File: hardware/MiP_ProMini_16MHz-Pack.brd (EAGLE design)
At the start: 41.4 x 63.8 mm, 52 parts, among them J2 AVR_ISP, Q1 16MHZ, U1 ATMEGA328, U2 MIC5205-5.0, U3 TS3USB221A, U4 MIC5205-3.3

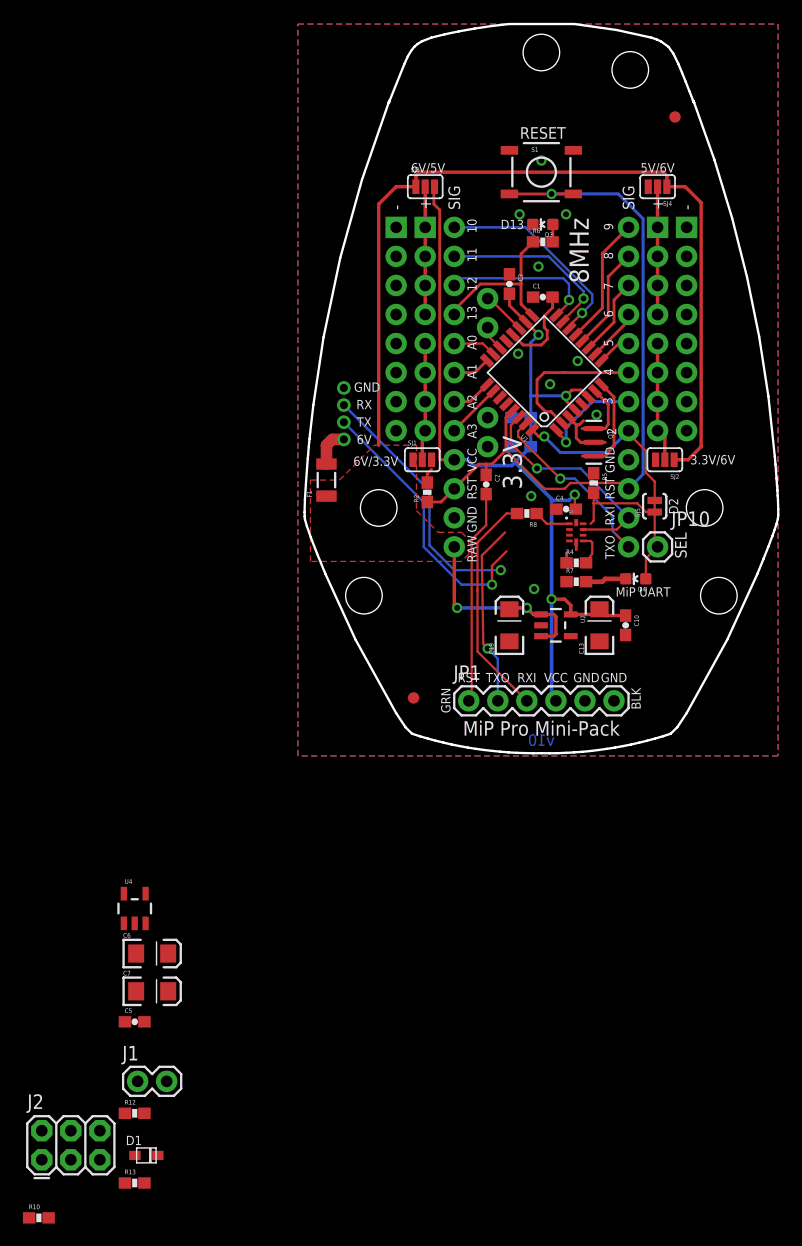
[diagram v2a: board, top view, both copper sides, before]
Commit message: Initial layout complete
No more air wires to route and passes OSHPark DRC.

Important notes:
* I had to move the A6/A7 1x2 jumper block to move the AVR up higher on
  the board. This was done to make more room for larger passives and an
  extra voltage regulator lower on the board.
* I ended up removing the AVR-ISP port since I couldn't fit it on the
  left side of the board where it would have been easy to route.
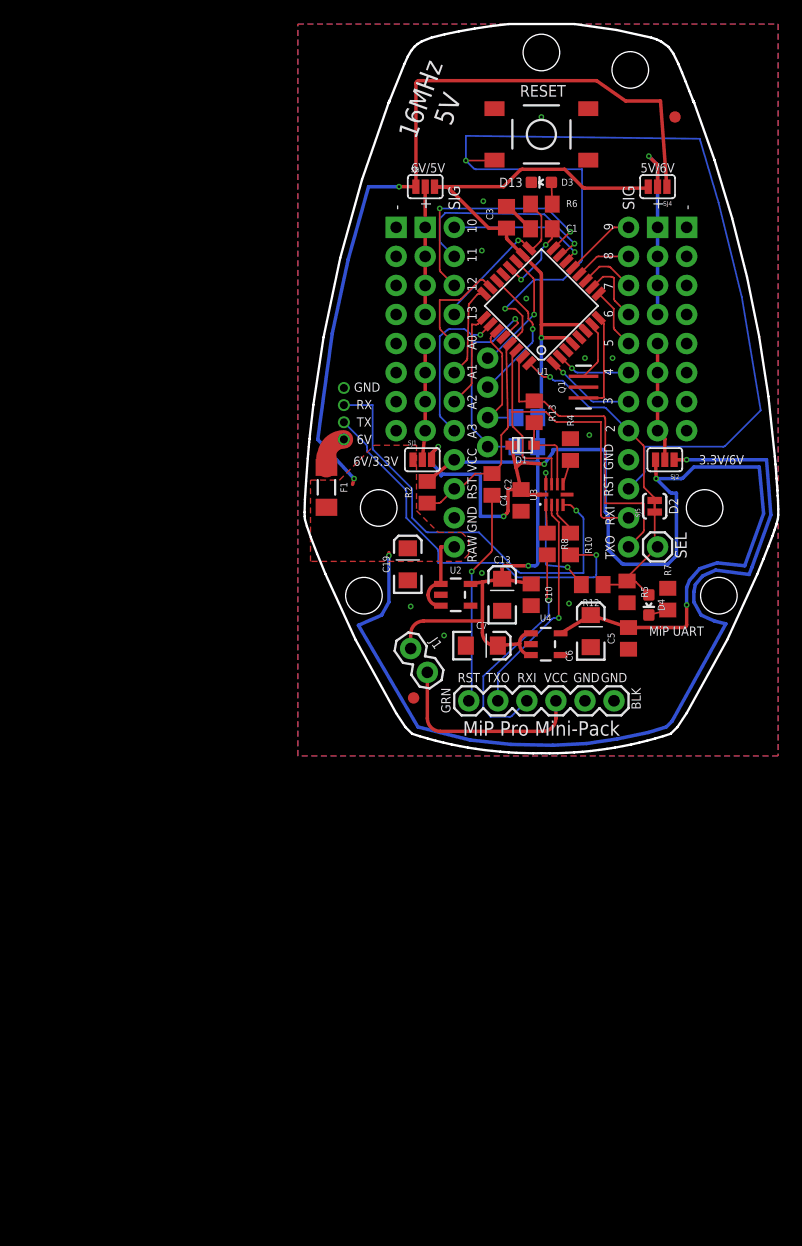
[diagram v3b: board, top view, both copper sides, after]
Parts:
- removed J2: AVR_ISP, SparkFun-Connectors:2X3
- C1, C10, C2, C3, C4, C5: device SparkFun-Capacitors:0603-CAP -> rcl:C0805
- F1: value PTCSMD -> PTCCUSTOM; device SparkFun-PowerIC:PTC-1206 -> adam_custom:PTC-1206-CUSTOM
- Q1: device SparkFun-FreqCtrl:RESONATOR-SMD -> adam_custom:RESONATOR-SMD-CUSTOM
- R1, R2, R3: device SparkFun:0603-RES -> rcl:R0805
- R10, R12, R13, R4, R5, R6, R7, R8: device SparkFun-Resistors:0603-RES -> rcl:R0805
- S1: device SparkFun-Electromechanical:TACTILE-SWITCH-SMD -> adam_custom:TACTILE-SWITCH-SMD-CKN9112CT-ND
- U3: device SparkFun-AnalogIC:QFN-10-RSE -> adam_custom:QFN-10-RSE-CUSTOM
- moved R13 75.9 mm to (20.7, 30.1), turned to 270 degrees
- moved R10 75.1 mm to (23.9, 18.5), turned to 270 degrees
- moved D1 70.3 mm to (19.7, 27.2), turned to 180 degrees
- moved R12 61.1 mm to (25.8, 15.0), turned to 180 degrees
- moved C5 54.7 mm to (29.0, 10.3), turned to 270 degrees
- moved C6 47.6 mm to (25.7, 10.9), turned to 90 degrees
- moved J1 44.7 mm to (9.91, 9.40), turned to 305 degrees
- moved U4 42.7 mm to (21.7, 9.78), turned to 270 degrees
- moved C7 41.8 mm to (16.1, 9.65)
- moved C19 10.4 mm to (9.65, 16.8)
- moved R5 9.96 mm to (28.8, 14.4), turned to 90 degrees
- moved R4 9.92 mm to (23.9, 26.8), turned to 270 degrees
- moved U2 9.16 mm to (13.8, 14.1)
- moved C13 8.92 mm to (17.9, 14.1)
- moved C10 8.68 mm to (20.4, 14.1)
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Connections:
- net 3.3V: now also SJ1.3, SJ2.3; no longer SJ3.3, SJ4.3
- net 5V: now also SJ3.3, SJ4.3; no longer J2.2, SJ1.3, SJ2.3
- net GND: no longer J2.6
- net MISO: no longer J2.1
- net MOSI: no longer J2.4
- net RESET: no longer J2.5
- net SCK: no longer J2.3
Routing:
- net 3.3V: track 0.00 -> 96.4 mm, vias 0 -> 5
- net VIN: track 95.7 -> 157.3 mm, vias 2 -> 4
- net RESET: track 64.6 -> 115.5 mm, vias 1 -> 2
- net A5: track 0.00 -> 19.1 mm, vias 0 -> 1
- net N$15: track 0.00 -> 17.7 mm
- net 5V: track 89.3 -> 104.7 mm, vias 4 -> 2
- net TXO_MIP: track 22.5 -> 37.8 mm
- net RXI: track 20.0 -> 33.4 mm, vias 1 -> 0
- net N$16: track 0.00 -> 12.9 mm, vias 0 -> 2
- net A4: track 0.00 -> 11.3 mm
- net TXO: track 17.3 -> 27.3 mm, vias 1 -> 0
- net A7: track 2.19 -> 12.2 mm, vias 0 -> 1
- net RXI_MIP: track 24.6 -> 34.1 mm
- net A3: track 4.88 -> 14.0 mm, vias 0 -> 1
- net MISO: track 13.9 -> 21.6 mm, vias 1 -> 2
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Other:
- board text added: "16MHz 5V"
- board text added: "Adam Green"
- board text added: "https://github.com/adamgreen/MiP_ProMini-Pack"
- board text added: "v2"
- board text removed: "3.3V"
- board text removed: "8MHz"
- board text removed: "Casey Kuhns"
- board text removed: "v10"

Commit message: Use consistent case for 1K resistor value
I had used 1k in some places and 1K in others so that 2 different items
showed up in BOM.
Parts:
- R12, R13: value 1k -> 1K
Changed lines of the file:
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@@
 <attribute name="VALUE" x="6.576753125" y="8.61721875" size="1.27" layer="27" rot="R305"/>
 </element>
-<element name="R12" library="rcl" package="R0805" value="1k" x="25.781" y="14.986" smashed="yes" rot="R180">
+<element name="R12" library="rcl" package="R0805" value="1K" x="25.781" y="14.986" smashed="yes" rot="R180">
 <attribute name="NAME" x="26.416" y="13.716" size="0.6096" layer="25" font="vector" rot="R180"/>
 </element>
@@
 <attribute name="NAME" x="19.58" y="25.897" size="0.6096" layer="25" font="vector" rot="R180" align="center"/>
 </element>
-<element name="R13" library="rcl" package="R0805" value="1k" x="20.701" y="30.099" smashed="yes" rot="R270">
+<element name="R13" library="rcl" package="R0805" value="1K" x="20.701" y="30.099" smashed="yes" rot="R270">
 <attribute name="NAME" x="21.971" y="30.734" size="0.6096" layer="25" font="vector" rot="R270"/>
 </element>
